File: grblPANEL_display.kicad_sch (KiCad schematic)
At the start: 16 parts, among them J501 ILI9488, Q501 Q_NPN_BEC - S8050

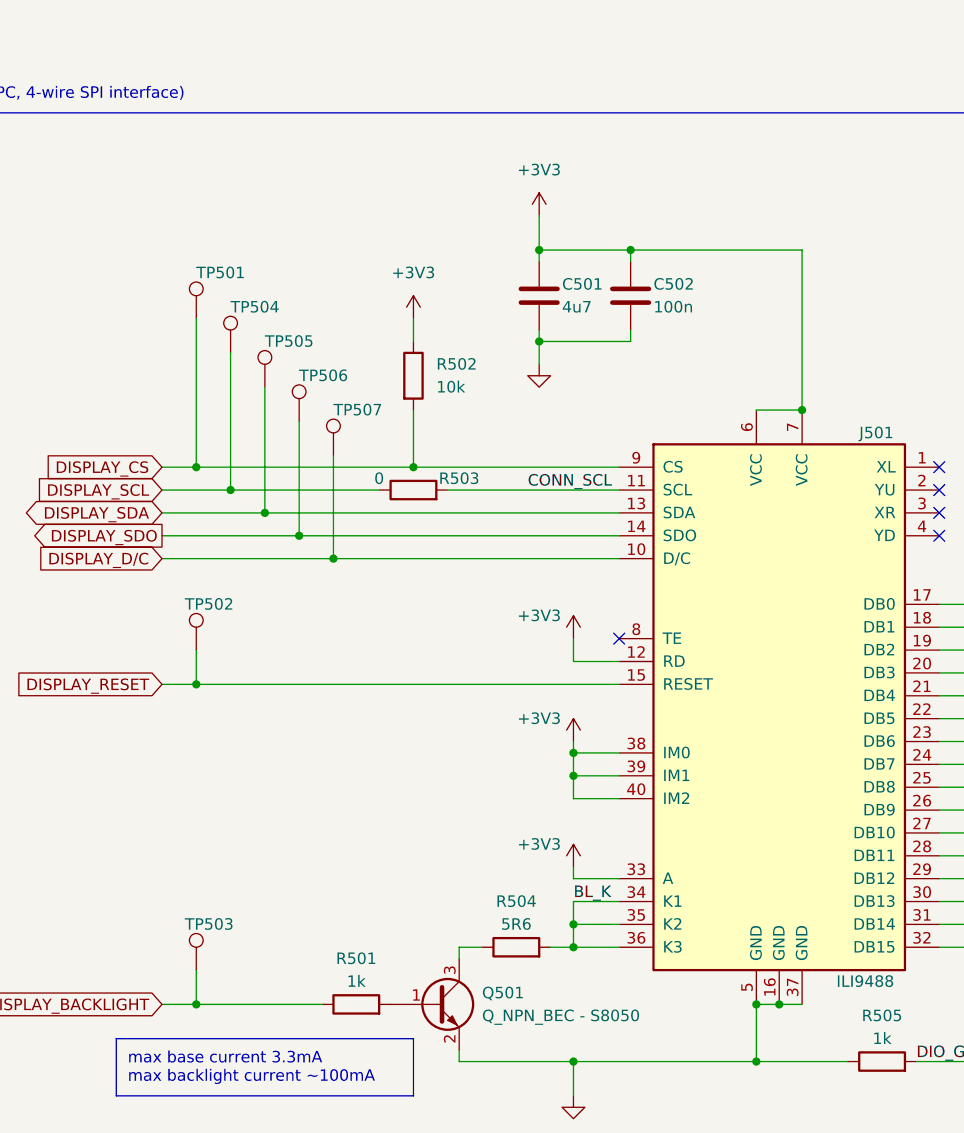
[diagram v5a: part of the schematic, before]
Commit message: keypad test points
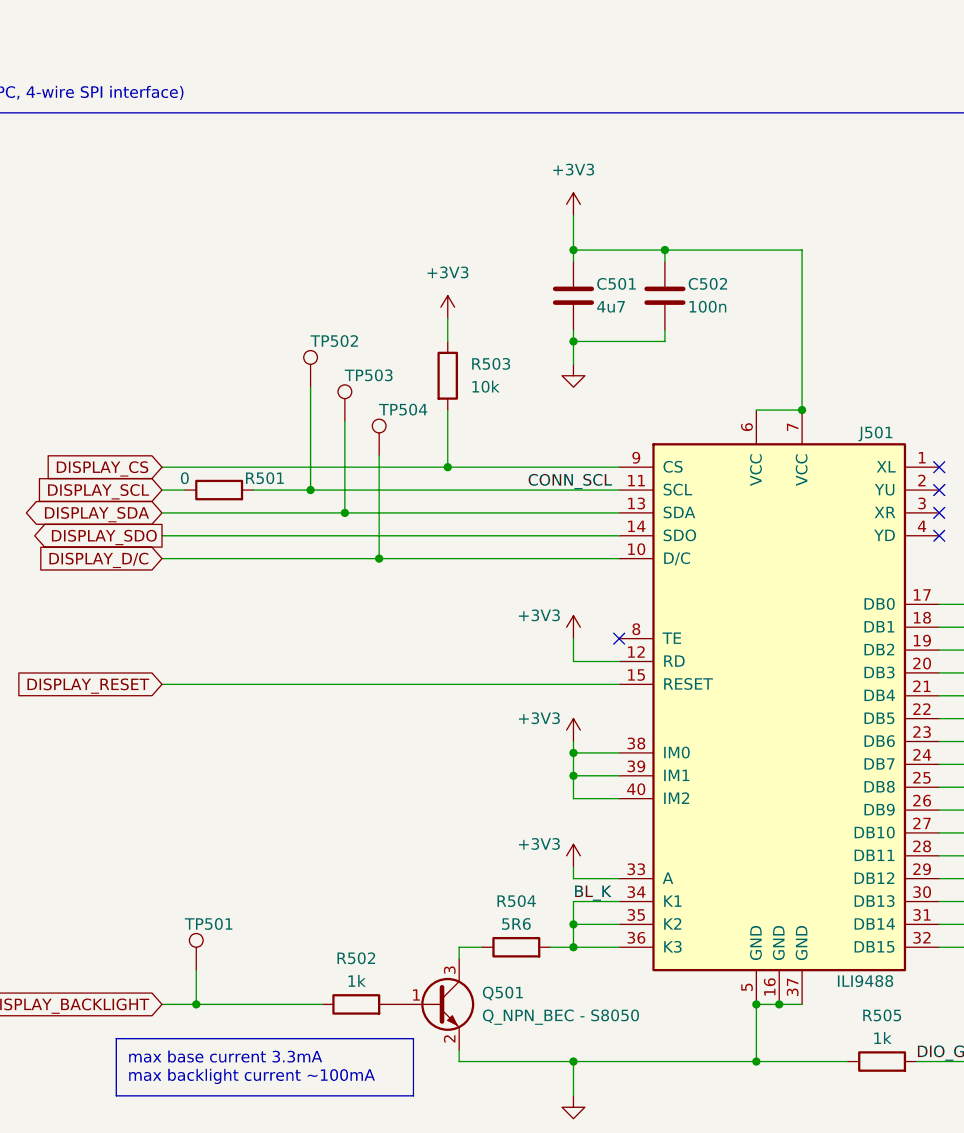
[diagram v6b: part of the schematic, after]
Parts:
- removed TP501, TP502, TP506: TestPoint, TestPoint:TestPoint_THTPad_D2.0mm_Drill1.0mm, symbol Connector:TestPoint
- renumbered R503 to R501, R501 to R502, R502 to R503, TP503 to TP501, TP504 to TP502, TP505 to TP503, TP507 to TP504
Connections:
- net CONN_SCL: now also TP502.1
- net DISPLAY_SCL: no longer TP502.1
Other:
- moved on the sheet: C501, C502, R501, R503, TP502, TP503, TP504

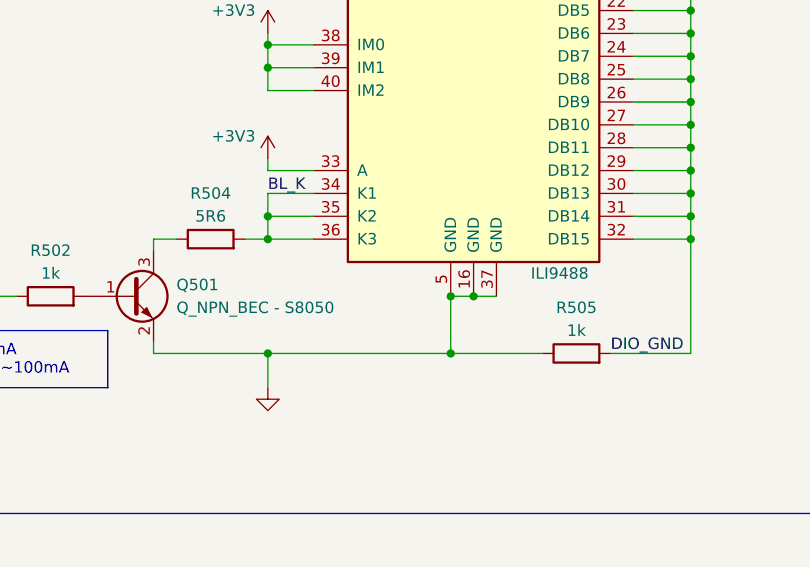
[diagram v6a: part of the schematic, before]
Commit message: Add mounting pads to ILI9488 connector symbol
Tied to ground plane in schematic and pcb
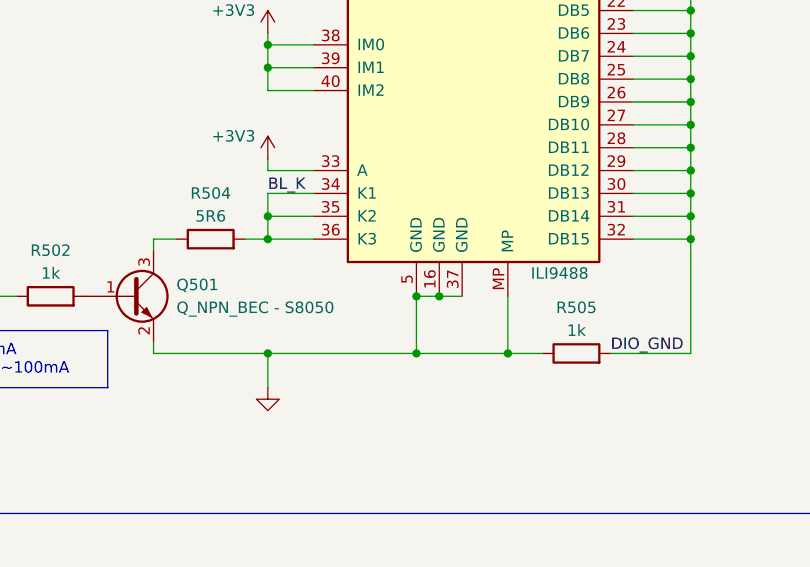
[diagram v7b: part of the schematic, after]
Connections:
- net GND: now also J501.MP
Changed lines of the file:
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@@
     (company "dresco")
   )
+  (junction (at 181.61 125.73) (diameter 0) (color 0 0 0 0)
+  )
   (junction (at 209.55 99.06) (diameter 0) (color 0 0 0 0)
   )
+  (junction (at 189.23 132.08) (diameter 0) (color 0 0 0 0)
+  )
   (junction (at 162.56 41.91) (diameter 0) (color 0 0 0 0)
   )
@@
   (junction (at 209.55 104.14) (diameter 0) (color 0 0 0 0)
   )
-  (junction (at 182.88 125.73) (diameter 0) (color 0 0 0 0)
-  )
   (junction (at 137.16 71.12) (diameter 0) (color 0 0 0 0)
   )
@@
   (junction (at 162.56 97.79) (diameter 0) (color 0 0 0 0)
   )
-  (junction (at 185.42 125.73) (diameter 0) (color 0 0 0 0)
-  )
   (junction (at 209.55 116.84) (diameter 0) (color 0 0 0 0)
   )
   (junction (at 120.65 125.73) (diameter 0) (color 0 0 0 0)
   )
+  (junction (at 179.07 125.73) (diameter 0) (color 0 0 0 0)
+  )
   (junction (at 148.59 66.04) (diameter 0) (color 0 0 0 0)
   )
@@
   (junction (at 162.56 100.33) (diameter 0) (color 0 0 0 0)
   )
-  (junction (at 182.88 132.08) (diameter 0) (color 0 0 0 0)
+  (junction (at 179.07 132.08) (diameter 0) (color 0 0 0 0)
   )
   (junction (at 133.35 68.58) (diameter 0) (color 0 0 0 0)
@@
     (stroke (width 0) (type default) (color 0 0 0 0))
   )
-  (wire (pts (xy 182.88 132.08) (xy 193.04 132.08))
+  (wire (pts (xy 179.07 132.08) (xy 189.23 132.08))
     (stroke (width 0) (type default) (color 0 0 0 0))
   )
@@
     (stroke (width 0) (type default) (color 0 0 0 0))
   )
-  (wire (pts (xy 162.56 132.08) (xy 182.88 132.08))
+  (wire (pts (xy 162.56 132.08) (xy 179.07 132.08))
     (stroke (width 0) (type default) (color 0 0 0 0))
   )
@@
     (stroke (width 0) (type default) (color 0 0 0 0))
   )
-  (wire (pts (xy 182.88 125.73) (xy 182.88 132.08))
+  (wire (pts (xy 179.07 125.73) (xy 179.07 132.08))
     (stroke (width 0) (type default) (color 0 0 0 0))
   )
@@
     (stroke (width 0) (type default) (color 0 0 0 0))
   )
+  (wire (pts (xy 189.23 132.08) (xy 193.04 132.08))
+    (stroke (width 0) (type default) (color 0 0 0 0))
+  )
   (polyline (pts (xy 77.47 26.67) (xy 233.68 26.67))
     (stroke (width 0) (type default) (color 0 0 0 0))
@@
     (stroke (width 0) (type default) (color 0 0 0 0))
   )
+  (wire (pts (xy 181.61 125.73) (xy 184.15 125.73))
+    (stroke (width 0) (type default) (color 0 0 0 0))
+  )
   (wire (pts (xy 209.55 111.76) (xy 209.55 114.3))
     (stroke (width 0) (type default) (color 0 0 0 0))
@@
     (stroke (width 0) (type default) (color 0 0 0 0))
   )
-  (wire (pts (xy 185.42 125.73) (xy 187.96 125.73))
-    (stroke (width 0) (type default) (color 0 0 0 0))
-  )
   (wire (pts (xy 203.2 101.6) (xy 209.55 101.6))
     (stroke (width 0) (type default) (color 0 0 0 0))
@@
     (stroke (width 0) (type default) (color 0 0 0 0))
   )
-  (wire (pts (xy 182.88 125.73) (xy 185.42 125.73))
+  (wire (pts (xy 179.07 125.73) (xy 181.61 125.73))
     (stroke (width 0) (type default) (color 0 0 0 0))
   )
@@
   )
   (wire (pts (xy 209.55 116.84) (xy 209.55 119.38))
+    (stroke (width 0) (type default) (color 0 0 0 0))
+  )
+  (wire (pts (xy 189.23 125.73) (xy 189.23 132.08))
     (stroke (width 0) (type default) (color 0 0 0 0))
   )
@@
     (pin "8")
     (pin "9")
+    (pin "MP")
   )
   (symbol (lib_id "power:GND") (at 162.56 135.89 0) (unit 1)
